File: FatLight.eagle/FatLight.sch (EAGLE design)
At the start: 27 parts, among them J1 12V, Q1 IRF540, Q2 IRF540, Q3 IRF540, Q4 16MHz, U1 ATMEGA328P-PU

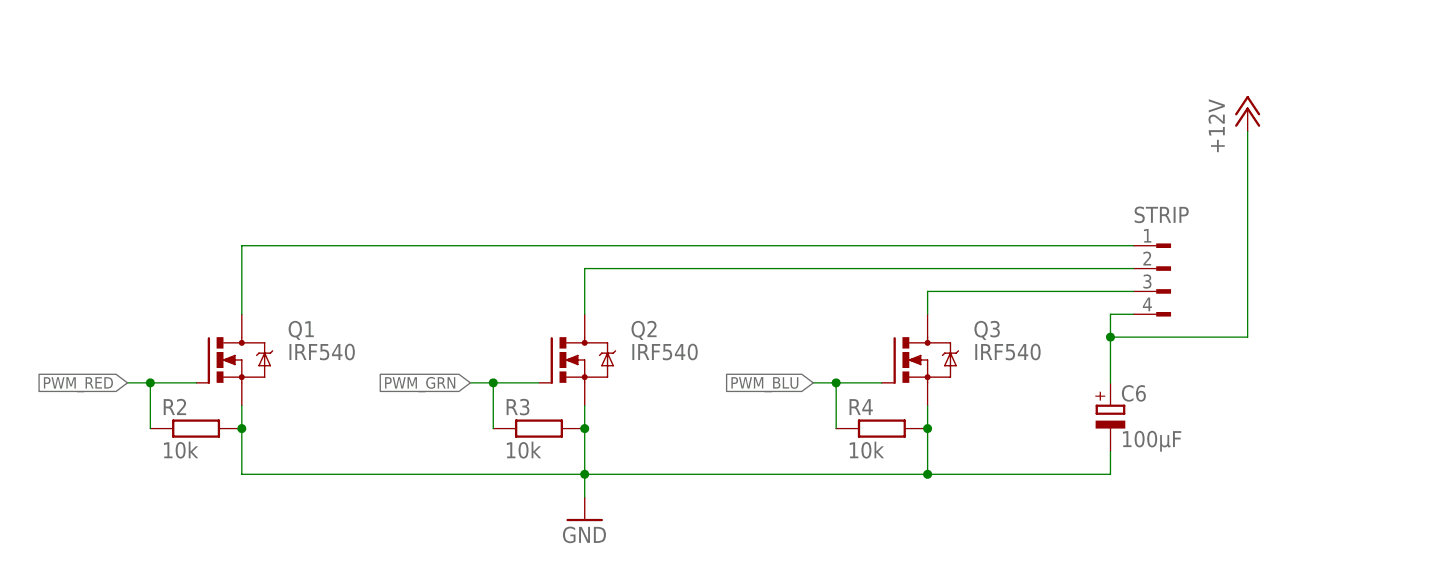
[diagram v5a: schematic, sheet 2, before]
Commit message: Neue Revision des Boards, Firmware mit Farbeffekten
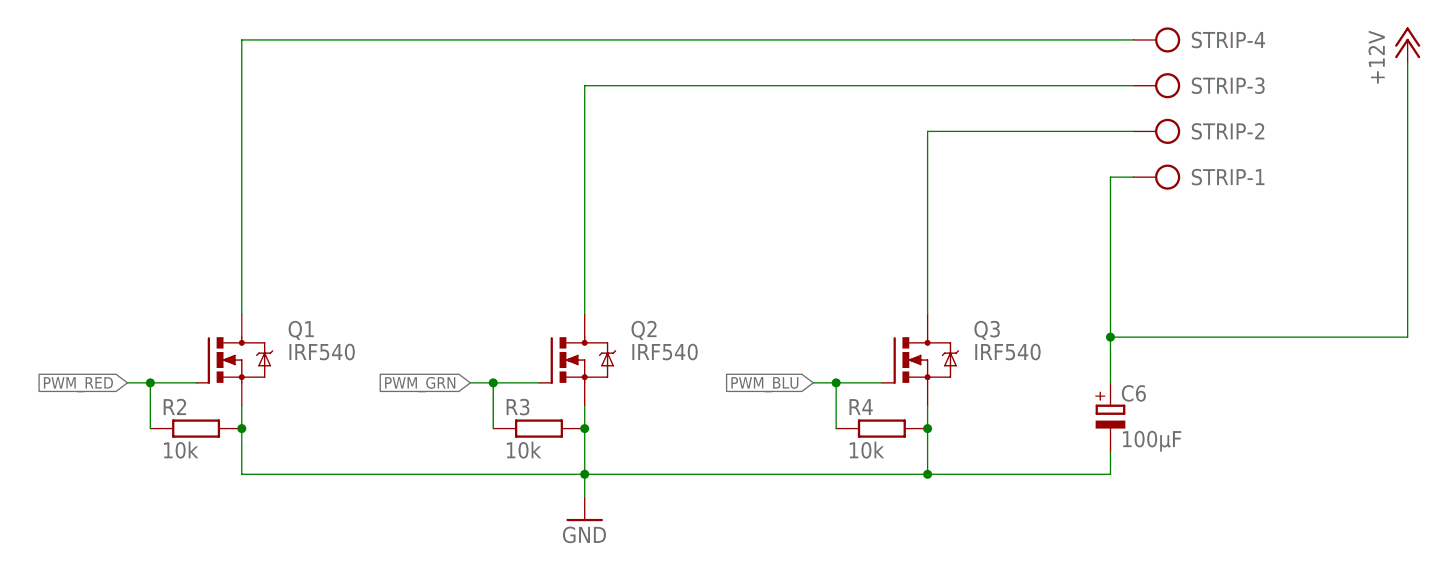
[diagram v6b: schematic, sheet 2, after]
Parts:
- removed J1: 12V, con-jack:JACK-PLUG0
- added POWER: (no value), con-ptr500:AK500/2
- STRIP: device con-amp:FLOP-4W -> con-ptr500:AK500/4
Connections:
- net +12V: now also POWER-2.KL, STRIP-1.KL; no longer J1.3, STRIP.4
- net GND: now also POWER-1.KL; no longer J1.1, J1.2
- net STRIP_BLU: now also STRIP-2.KL; no longer STRIP.3
- net STRIP_GRN: now also STRIP-3.KL; no longer STRIP.2
- net STRIP_RED: now also STRIP-4.KL; no longer STRIP.1
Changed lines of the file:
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@@
 <part name="FRAME1" library="frames" deviceset="A4L-LOC" device="" value="Prozessor"/>
 <part name="FRAME2" library="frames" deviceset="A4L-LOC" device="" value="PWM"/>
-<part name="STRIP" library="con-amp" deviceset="FLOP-4W" device=""/>
 <part name="P+4" library="supply1" deviceset="+12V" device=""/>
 <part name="FRAME3" library="frames" deviceset="A4L-LOC" device="" value="Power"/>
 <part name="SD1" library="Zap-Powerconverters" deviceset="D-SUN-STEPDOWN" device=""/>
-<part name="J1" library="con-jack" deviceset="JACK-PLUG" device="0" value="12V"/>
 <part name="C5" library="rcl" deviceset="CPOL-EU" device="E2.5-5" value="100µF"/>
 <part name="P+5" library="supply1" deviceset="+5V" device=""/>
@@
 <part name="C7" library="rcl" deviceset="CPOL-EU" device="E2.5-5" value="100µF"/>
 <part name="C8" library="rcl" deviceset="C-EU" device="025-025X050" value="100nF"/>
+<part name="STRIP" library="con-ptr500" deviceset="AK500/4" device=""/>
+<part name="POWER" library="con-ptr500" deviceset="AK500/2" device=""/>
 </parts>
 <sheets>
@@
 <instance part="GND7" gate="1" x="93.98" y="63.5"/>
 <instance part="FRAME2" gate="G$1" x="0" y="0"/>
-<instance part="STRIP" gate="G$1" x="157.48" y="88.9"/>
-<instance part="P+4" gate="1" x="167.64" y="109.22"/>
+<instance part="P+4" gate="1" x="185.42" y="116.84"/>
 <instance part="C6" gate="G$1" x="152.4" y="76.2"/>
+<instance part="STRIP" gate="-1" x="160.02" y="101.6" rot="R180"/>
+<instance part="STRIP" gate="-2" x="160.02" y="106.68" rot="R180"/>
+<instance part="STRIP" gate="-3" x="160.02" y="111.76" rot="R180"/>
+<instance part="STRIP" gate="-4" x="160.02" y="116.84" rot="R180"/>
 </instances>
 <busses>
@@
 <segment>
 <pinref part="Q3" gate="G$1" pin="D"/>
-<pinref part="STRIP" gate="G$1" pin="3"/>
-<wire x1="154.94" y1="88.9" x2="132.08" y2="88.9" width="0.1524" layer="91"/>
-<wire x1="132.08" y1="88.9" x2="132.08" y2="86.36" width="0.1524" layer="91"/>
+<wire x1="132.08" y1="86.36" x2="132.08" y2="106.68" width="0.1524" layer="91"/>
+<pinref part="STRIP" gate="-2" pin="KL"/>
+<wire x1="132.08" y1="106.68" x2="154.94" y2="106.68" width="0.1524" layer="91"/>
 </segment>
 </net>
@@
 <segment>
 <pinref part="Q1" gate="G$1" pin="D"/>
-<pinref part="STRIP" gate="G$1" pin="1"/>
-<wire x1="154.94" y1="93.98" x2="55.88" y2="93.98" width="0.1524" layer="91"/>
-<wire x1="55.88" y1="93.98" x2="55.88" y2="86.36" width="0.1524" layer="91"/>
+<wire x1="55.88" y1="116.84" x2="55.88" y2="86.36" width="0.1524" layer="91"/>
+<pinref part="STRIP" gate="-4" pin="KL"/>
+<wire x1="154.94" y1="116.84" x2="55.88" y2="116.84" width="0.1524" layer="91"/>
 </segment>
 </net>
@@
 <segment>
 <pinref part="Q2" gate="G$1" pin="D"/>
-<pinref part="STRIP" gate="G$1" pin="2"/>
-<wire x1="154.94" y1="91.44" x2="93.98" y2="91.44" width="0.1524" layer="91"/>
-<wire x1="93.98" y1="91.44" x2="93.98" y2="86.36" width="0.1524" layer="91"/>
+<wire x1="93.98" y1="86.36" x2="93.98" y2="111.76" width="0.1524" layer="91"/>
+<pinref part="STRIP" gate="-3" pin="KL"/>
+<wire x1="93.98" y1="111.76" x2="154.94" y2="111.76" width="0.1524" layer="91"/>
 </segment>
 </net>
@@
 <segment>
 <pinref part="P+4" gate="1" pin="+12V"/>
-<wire x1="152.4" y1="86.36" x2="152.4" y2="83.82" width="0.1524" layer="91"/>
-<wire x1="152.4" y1="83.82" x2="167.64" y2="83.82" width="0.1524" layer="91"/>
-<wire x1="167.64" y1="83.82" x2="167.64" y2="106.68" width="0.1524" layer="91"/>
-<pinref part="STRIP" gate="G$1" pin="4"/>
-<wire x1="152.4" y1="86.36" x2="154.94" y2="86.36" width="0.1524" layer="91"/>
+<wire x1="152.4" y1="83.82" x2="185.42" y2="83.82" width="0.1524" layer="91"/>
+<wire x1="185.42" y1="83.82" x2="185.42" y2="114.3" width="0.1524" layer="91"/>
 <pinref part="C6" gate="G$1" pin="+"/>
 <wire x1="152.4" y1="78.74" x2="152.4" y2="83.82" width="0.1524" layer="91"/>
 <junction x="152.4" y="83.82"/>
+<wire x1="152.4" y1="83.82" x2="152.4" y2="101.6" width="0.1524" layer="91"/>
+<pinref part="STRIP" gate="-1" pin="KL"/>
+<wire x1="152.4" y1="101.6" x2="154.94" y2="101.6" width="0.1524" layer="91"/>
 </segment>
 </net>
@@
 <instance part="FRAME3" gate="G$1" x="0" y="0"/>
 <instance part="SD1" gate="A" x="106.68" y="124.46" rot="MR180"/>
-<instance part="J1" gate="G$1" x="71.12" y="127"/>
 <instance part="C5" gate="G$1" x="127" y="127"/>
 <instance part="P+5" gate="1" x="127" y="147.32"/>
@@
 <instance part="GND8" gate="1" x="86.36" y="109.22"/>
 <instance part="P+6" gate="1" x="86.36" y="147.32"/>
+<instance part="POWER" gate="-1" x="73.66" y="121.92"/>
+<instance part="POWER" gate="-2" x="73.66" y="129.54"/>
 </instances>
 <busses>
@@
 <net name="GND" class="0">
 <segment>
-<pinref part="J1" gate="G$1" pin="2"/>
-<wire x1="76.2" y1="127" x2="86.36" y2="127" width="0.1524" layer="91"/>
 <pinref part="GND8" gate="1" pin="GND"/>
 <wire x1="86.36" y1="111.76" x2="86.36" y2="121.92" width="0.1524" layer="91"/>
 <pinref part="SD1" gate="A" pin="IN-2"/>
-<wire x1="86.36" y1="121.92" x2="86.36" y2="127" width="0.1524" layer="91"/>
 <wire x1="91.44" y1="121.92" x2="86.36" y2="121.92" width="0.1524" layer="91"/>
-<junction x="86.36" y="121.92"/>
 <pinref part="SD1" gate="A" pin="IN-1"/>
 <wire x1="91.44" y1="121.92" x2="91.44" y2="119.38" width="0.1524" layer="91"/>
 <junction x="91.44" y="121.92"/>
-<pinref part="J1" gate="G$1" pin="1"/>
-<wire x1="76.2" y1="127" x2="76.2" y2="124.46" width="0.1524" layer="91"/>
-<junction x="76.2" y="127"/>
+<pinref part="POWER" gate="-1" pin="KL"/>
+<wire x1="86.36" y1="121.92" x2="78.74" y2="121.92" width="0.1524" layer="91"/>
+<junction x="86.36" y="121.92"/>
 </segment>
 <segment>
@@
 <segment>
 <pinref part="P+6" gate="1" pin="+12V"/>
-<pinref part="J1" gate="G$1" pin="3"/>
-<wire x1="76.2" y1="129.54" x2="86.36" y2="129.54" width="0.1524" layer="91"/>
 <pinref part="SD1" gate="A" pin="IN+2"/>
 <wire x1="86.36" y1="129.54" x2="91.44" y2="129.54" width="0.1524" layer="91"/>
 <wire x1="86.36" y1="129.54" x2="86.36" y2="144.78" width="0.1524" layer="91"/>
-<junction x="86.36" y="129.54"/>
 <pinref part="SD1" gate="A" pin="IN+1"/>
 <wire x1="91.44" y1="129.54" x2="91.44" y2="127" width="0.1524" layer="91"/>
 <junction x="91.44" y="129.54"/>
-</segment>
-</net>
+<pinref part="POWER" gate="-2" pin="KL"/>
+<wire x1="86.36" y1="129.54" x2="78.74" y2="129.54" width="0.1524" layer="91"/>
+<junction x="86.36" y="129.54"/>
+</segment>
+</net>
